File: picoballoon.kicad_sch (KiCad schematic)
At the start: 97 parts, among them J1 SOLAR+, J2 SOLAR-, J3 USB_B_Micro, Q1 AO3401A, Q2 AO3401A, Q3 DTC143ZEBTL, Q4 DTC143ZEBTL, Q5 AO3401A, U1 SPV1040, U2 AMS1117-3.3, U3 DHT11, U4 STM32G070RBTx, U6 GPS1003, U7 Ai-Thinker-Ra-01, U8 L70-R, Y1 Crystal

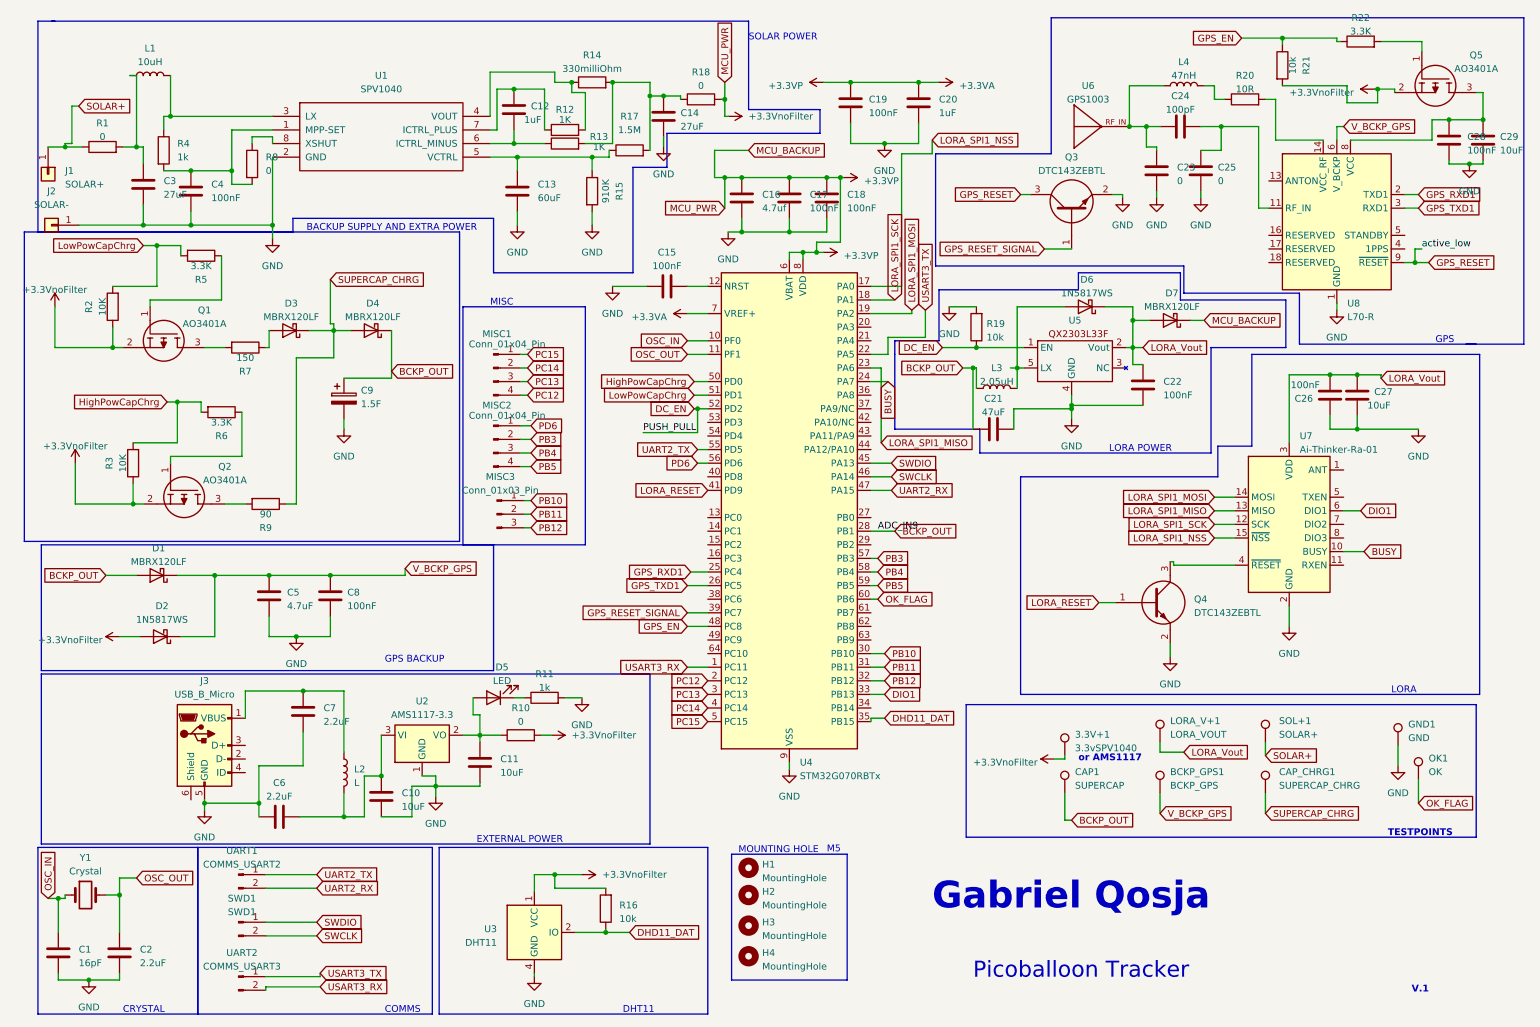
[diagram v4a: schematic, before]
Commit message: PCB completed and is in production
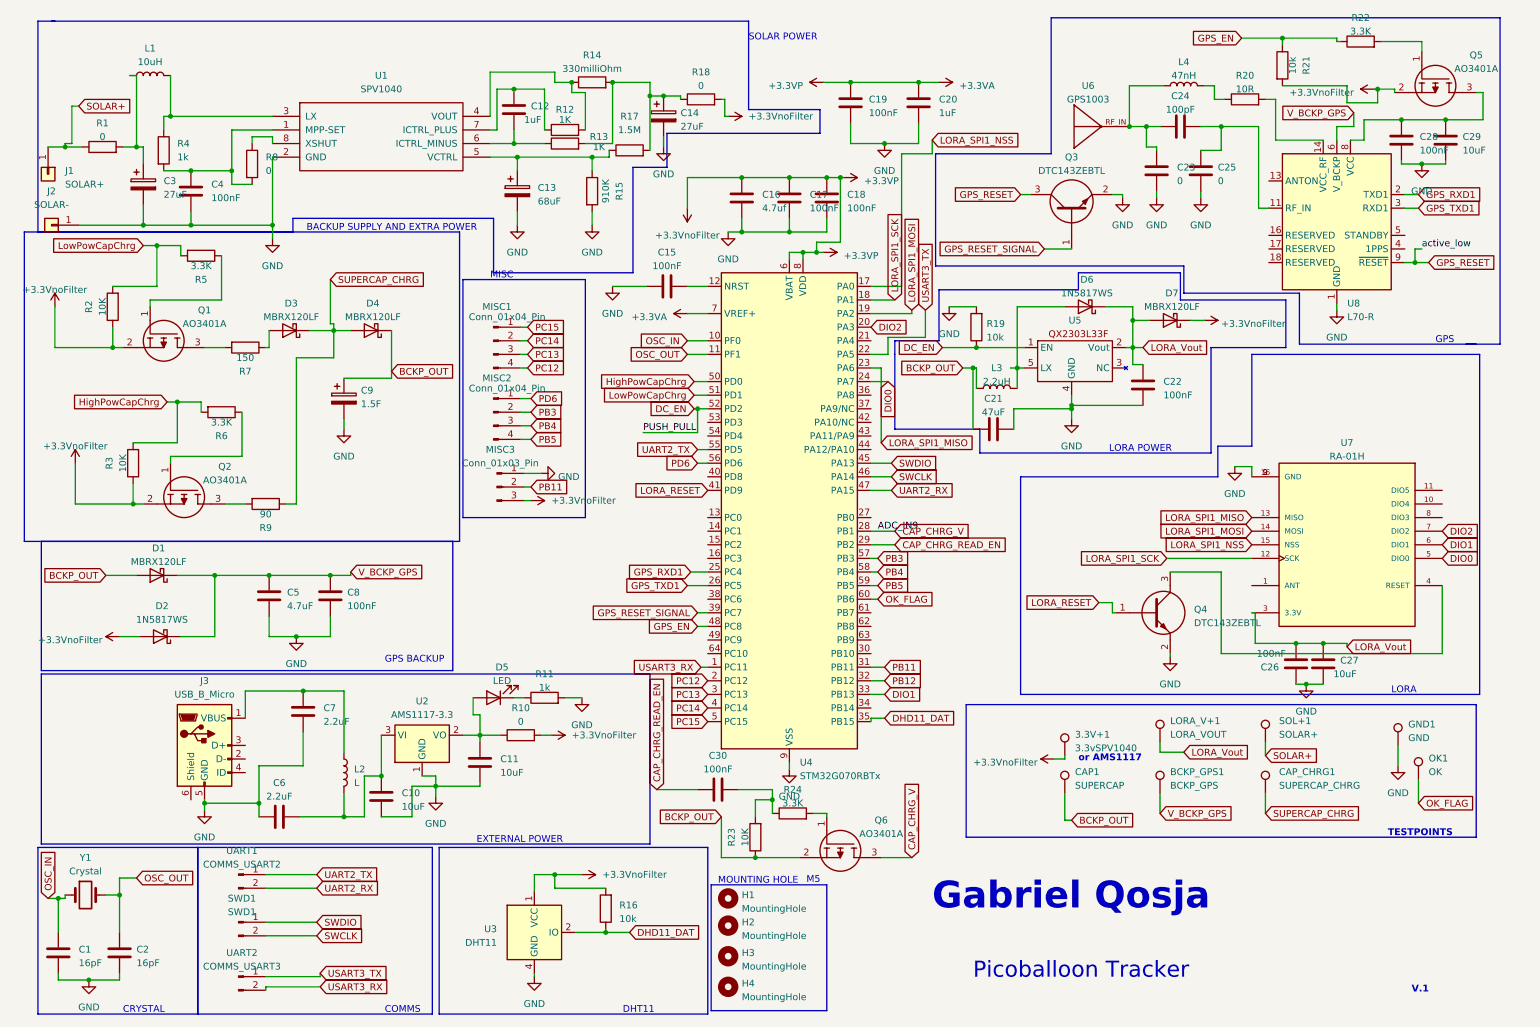
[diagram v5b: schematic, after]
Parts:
- removed U7: Ai-Thinker-Ra-01, RF_Module:Ai-Thinker-Ra-01-LoRa, symbol RF_Module:Ai-Thinker-Ra-01
- added C30: 100nF, Capacitor_SMD:C_0603_1608Metric, symbol Device:C
- added Q6: AO3401A, Package_TO_SOT_SMD:SOT-23, symbol AO3401A:AO3401A
- added R23: 10K, Resistor_THT:R_Axial_DIN0204_L3.6mm_D1.6mm_P2.54mm_Vertical, symbol Device:R
- added R24: 3.3K, Resistor_SMD:R_0603_1608Metric, symbol Device:R
- added U7: RA-01H, RF_Module:Ai-Thinker-Ra-01-LoRa, symbol RA-01H:RA-01H
- C13: value 60uF -> 68uF; footprint Capacitor_SMD:C_0603_1608Metric -> Capacitor_THT:C_Radial_D5.0mm_H11.0mm_P2.00mm; symbol Device:C -> Device:C_Polarized
- C14, C3: footprint Capacitor_SMD:C_0603_1608Metric -> Capacitor_THT:C_Radial_D5.0mm_H11.0mm_P2.00mm; symbol Device:C -> Device:C_Polarized
- C2: value 2.2uF -> 16pF
- C23, C25: footprint Capacitor_SMD:C_0603_1608Metric -> Resistor_SMD:R_0603_1608Metric
- L3: value 2,05uH -> 2,2uH
- R1, R10, R18, R8: footprint Resistor_SMD:R_0603_1608Metric -> Resistor_SMD:R_1210_3225Metric
- R14: footprint Resistor_SMD:R_0603_1608Metric -> Resistor_SMD:R_2512_6332Metric
- R7, R9: footprint Resistor_SMD:R_0603_1608Metric -> Resistor_SMD:R_1206_3216Metric
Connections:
- net +3.3V: now also MISC3.3 (Pin_3)
- net BCKP_OUT: now also Q6.2, R23.1; no longer U4.28 (PB1)
- net DIO1: now also U7.6 (DIO1)
- net GND: now also MISC3.1 (Pin_1), U7.16 (GND), U7.2 (GND), U7.9 (GND)
- net LORA_SPI1_MISO: now also U7.13 (MISO)
- net LORA_SPI1_MOSI: now also U7.14 (MOSI)
- net LORA_SPI1_NSS: now also U7.15 (NSS)
- net LORA_SPI1_SCK: now also U7.12 (SCK)
- net LORA_Vout: now also U7.3 (3.3V)
- net PB12: no longer MISC3.3 (Pin_3)
- net DIO2: now reaches U4.20 (PA3)
- net DIO2: now also U7.7 (DIO2)
- net CAP_CHRG_READ_EN: now reaches U4.29 (PB2)
- net CAP_CHRG_READ_EN: now also C30.1
- net at Q4.3: now also U7.4 (RESET)
- net BUSY renamed DIO0
- net DIO0: now also U7.5 (DIO0)
- net PB10: no longer names the net of U4.30 (PB10)
- net PB10: no longer MISC3.1 (Pin_1)
- new net: C30.2, R23.2, R24.1
- new net: Q6.1, R24.2
- new net CAP_CHRG_V: Q6.3, U4.28 (PB1)
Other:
- moved on the sheet: C26, C27, C28, C29, H1, H2, H3, H4, MISC1, MISC2, MISC3, Q4
